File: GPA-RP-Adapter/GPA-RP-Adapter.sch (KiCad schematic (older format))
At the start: 8 parts

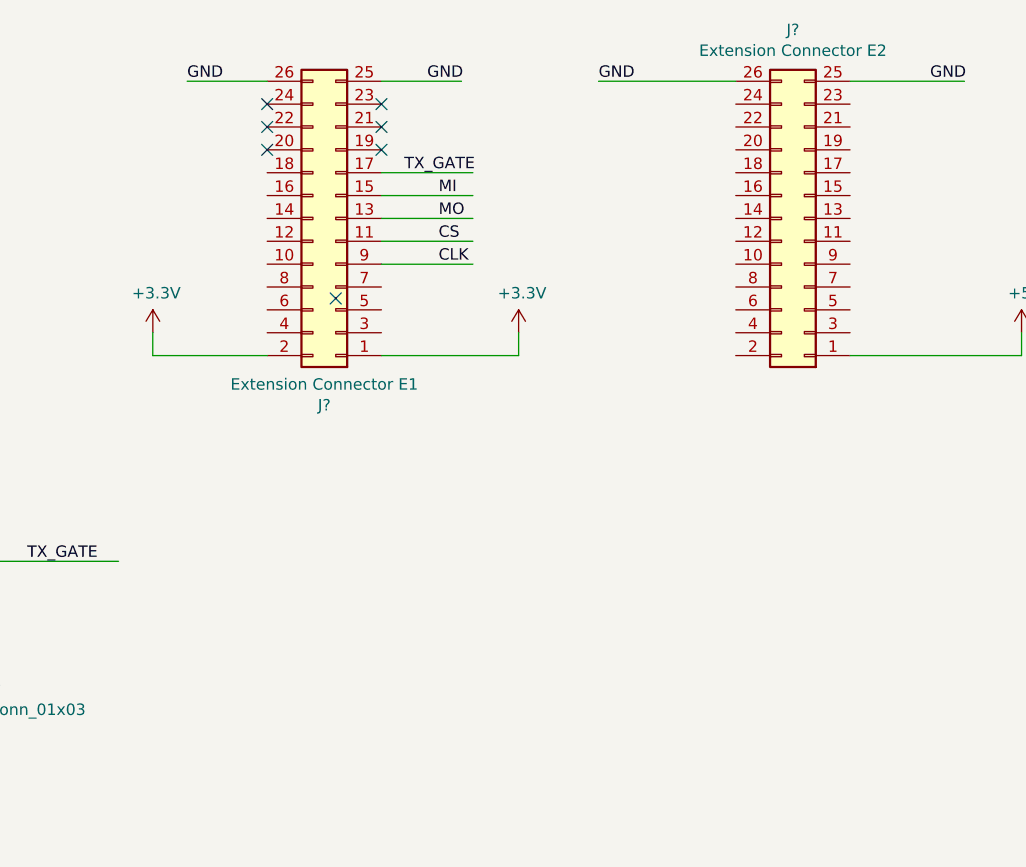
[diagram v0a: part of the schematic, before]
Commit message: added 2nd tx_gate
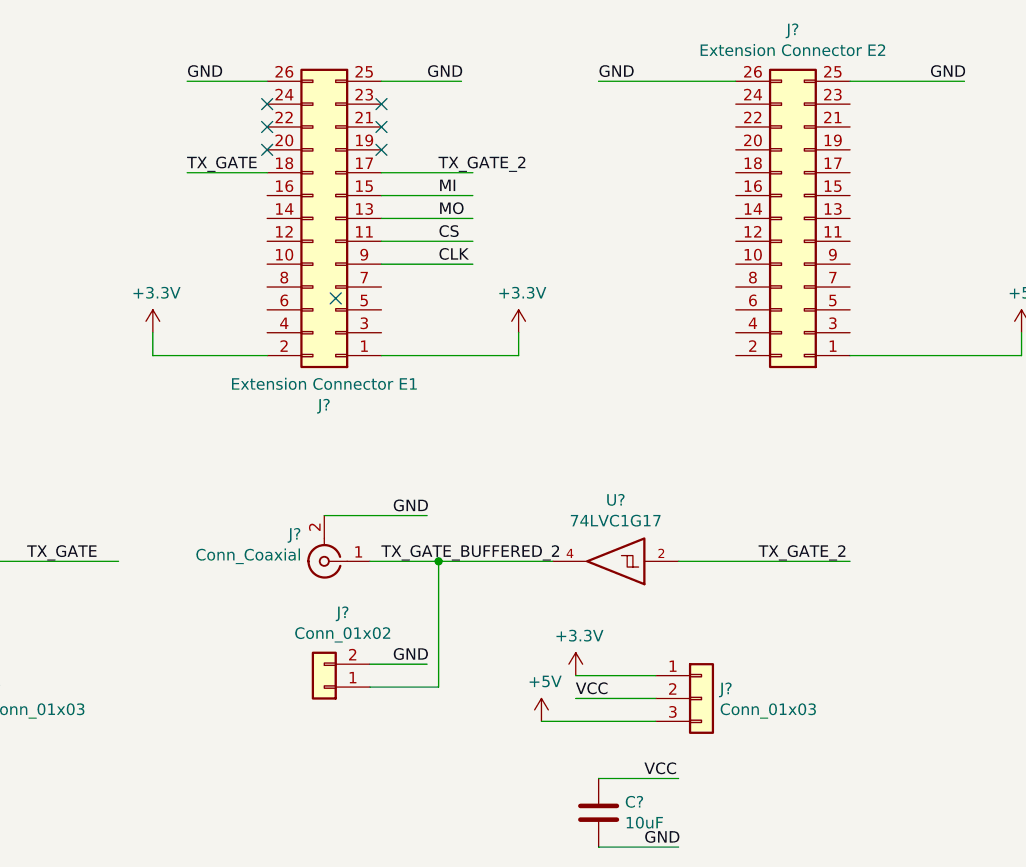
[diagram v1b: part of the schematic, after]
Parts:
- added C?: 10uF, symbol Device:C
- added J?: Conn_Coaxial, symbol Connector:Conn_Coaxial
- added J?: Conn_01x03, symbol Connector_Generic:Conn_01x03
- added J?: Conn_01x02, symbol Connector_Generic:Conn_01x02
- added U?: 74LVC1G17, symbol 74xGxx:74LVC1G17
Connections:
- net labels added: TX_GATE_2, TX_GATE_BUFFERED_2
- wire segments 38 -> 51
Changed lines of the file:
@@
 Text Label 1550 3200 0    50   ~ 0
 TX_GATE_BUFFERED
-Wire Wire Line
-	4750 1500 5150 1500
-Text Label 4850 1500 0    50   ~ 0
-TX_GATE
 $Comp
 L 74xGxx:74LVC1G17 U?
@@
 Wire Wire Line
 	1800 3200 2300 3200
+Wire Wire Line
+	4250 1500 3900 1500
+Text Label 3900 1500 0    50   ~ 0
+TX_GATE
+Wire Wire Line
+	4750 1500 5150 1500
+Text Label 5000 1500 0    50   ~ 0
+TX_GATE_2
+$Comp
+L Connector:Conn_Coaxial J?
+U 1 1 5F8539A5
+P 4500 3200
+F 0 "J?" H 4600 3082 50  0000 L CNN
+F 1 "Conn_Coaxial" H 4600 3173 50  0000 L CNN
+F 2 "" H 4500 3200 50  0001 C CNN
+F 3 " ~" H 4500 3200 50  0001 C CNN
+	1    4500 3200
+	-1   0    0    1
+$EndComp
+Wire Wire Line
+	4500 3000 4950 3000
+Text Label 4800 3000 0    50   ~ 0
+GND
+Text Label 4750 3200 0    50   ~ 0
+TX_GATE_BUFFERED_2
+$Comp
+L 74xGxx:74LVC1G17 U?
+U 1 1 5F8539AE
+P 5750 3200
+F 0 "U?" H 5725 2933 50  0000 C CNN
+F 1 "74LVC1G17" H 5725 3024 50  0000 C CNN
+F 2 "" H 5750 3200 50  0001 C CNN
+F 3 "http://www.ti.com/lit/sg/scyt129e/scyt129e.pdf" H 5750 3200 50  0001 C CNN
+	1    5750 3200
+	-1   0    0    1
+$EndComp
+Wire Wire Line
+	6050 3200 6800 3200
+Text Label 6400 3200 0    50   ~ 0
+TX_GATE_2
+$Comp
+L Connector_Generic:Conn_01x03 J?
+U 1 1 5F8539B6
+P 6150 3800
+F 0 "J?" H 6230 3842 50  0000 L CNN
+F 1 "Conn_01x03" H 6230 3751 50  0000 L CNN
+F 2 "" H 6150 3800 50  0001 C CNN
+F 3 "~" H 6150 3800 50  0001 C CNN
+	1    6150 3800
+	1    0    0    -1
+$EndComp
+Wire Wire Line
+	5950 3800 5600 3800
+Text Label 5600 3800 0    50   ~ 0
+VCC
+Wire Wire Line
+	5950 3700 5600 3700
+$Comp
+L power:+3.3V #PWR?
+U 1 1 5F8539BF
+P 5600 3700
+F 0 "#PWR?" H 5600 3550 50  0001 C CNN
+F 1 "+3.3V" H 5615 3873 50  0000 C CNN
+F 2 "" H 5600 3700 50  0001 C CNN
+F 3 "" H 5600 3700 50  0001 C CNN
+	1    5600 3700
+	1    0    0    -1
+$EndComp
+$Comp
+L power:+5V #PWR?
+U 1 1 5F8539C5
+P 5450 3900
+F 0 "#PWR?" H 5450 3750 50  0001 C CNN
+F 1 "+5V" H 5465 4073 50  0000 C CNN
+F 2 "" H 5450 3900 50  0001 C CNN
+F 3 "" H 5450 3900 50  0001 C CNN
+	1    5450 3900
+	1    0    0    -1
+$EndComp
+Wire Wire Line
+	5450 3900 5950 3900
+$Comp
+L Device:C C?
+U 1 1 5F8539CC
+P 5700 4300
+F 0 "C?" H 5815 4346 50  0000 L CNN
+F 1 "10uF" H 5815 4255 50  0000 L CNN
+F 2 "" H 5738 4150 50  0001 C CNN
+F 3 "~" H 5700 4300 50  0001 C CNN
+	1    5700 4300
+	1    0    0    -1
+$EndComp
+Wire Wire Line
+	5700 4150 6050 4150
+Wire Wire Line
+	5700 4450 6050 4450
+Text Label 5900 4150 0    50   ~ 0
+VCC
+Text Label 5900 4450 0    50   ~ 0
+GND
+$Comp
+L Connector_Generic:Conn_01x02 J?
+U 1 1 5F8539D6
+P 4500 3750
+F 0 "J?" H 4418 3425 50  0000 C CNN
+F 1 "Conn_01x02" H 4418 3516 50  0000 C CNN
+F 2 "" H 4500 3750 50  0001 C CNN
+F 3 "~" H 4500 3750 50  0001 C CNN
+	1    4500 3750
+	-1   0    0    1
+$EndComp
+Wire Wire Line
+	4700 3750 5000 3750
+Wire Wire Line
+	4700 3650 4950 3650
+Text Label 4800 3650 0    50   ~ 0
+GND
+Wire Wire Line
+	5000 3750 5000 3200
+Wire Wire Line
+	4700 3200 5000 3200
+Connection ~ 5000 3200
+Wire Wire Line
+	5000 3200 5500 3200
 $EndSCHEMATC

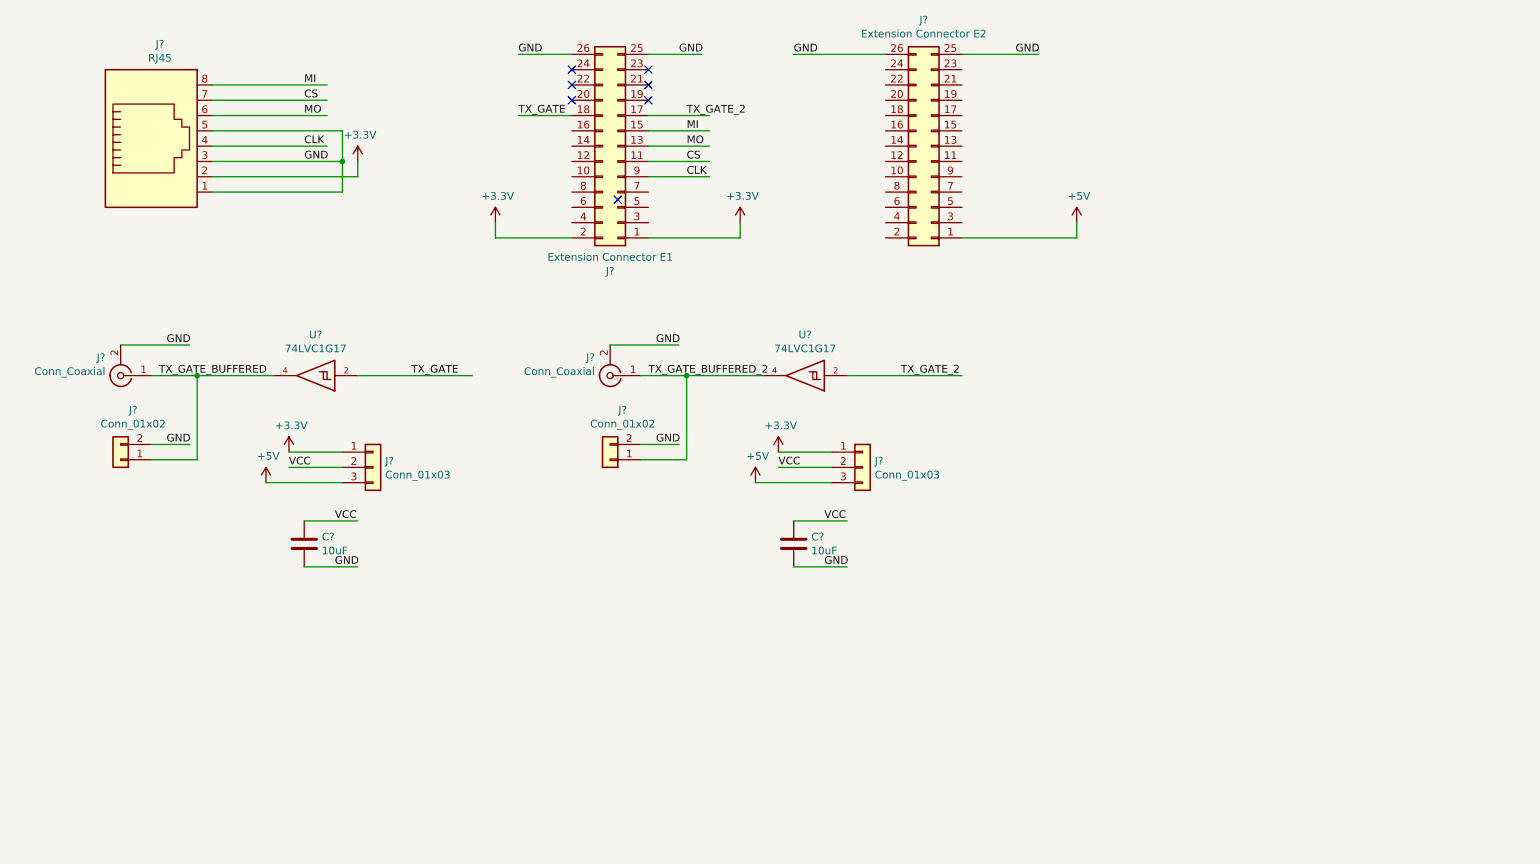
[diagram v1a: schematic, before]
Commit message: added analog IOs, SPI and fan
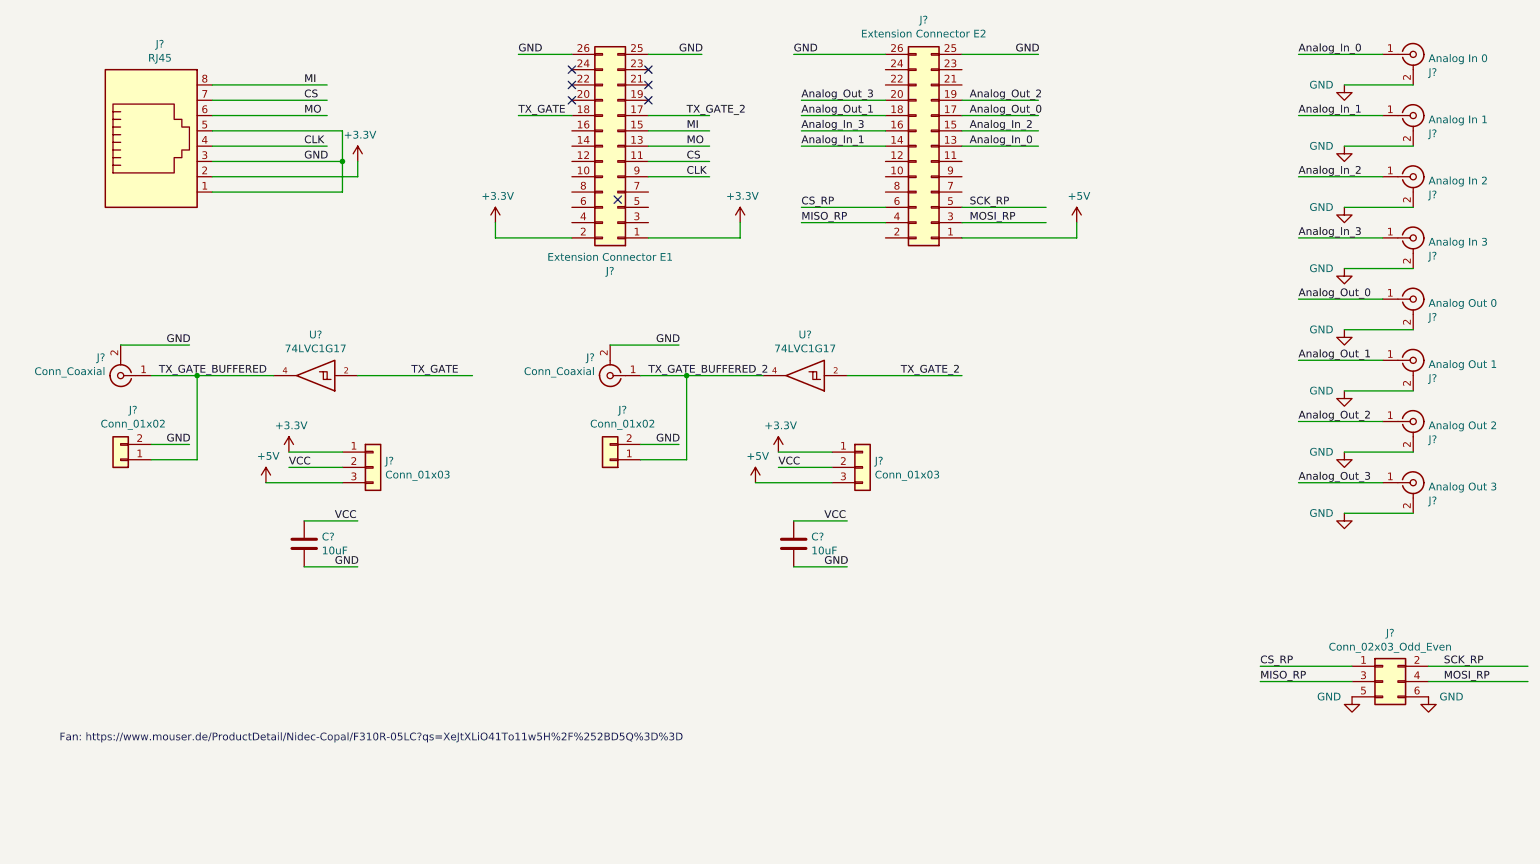
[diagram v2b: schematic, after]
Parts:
- added J?: Analog In 0, symbol Connector:Conn_Coaxial
- added J?: Analog In 1, symbol Connector:Conn_Coaxial
- added J?: Analog In 2, symbol Connector:Conn_Coaxial
- added J?: Analog In 3, symbol Connector:Conn_Coaxial
- added J?: Analog Out 0, symbol Connector:Conn_Coaxial
- added J?: Analog Out 1, symbol Connector:Conn_Coaxial
- added J?: Analog Out 2, symbol Connector:Conn_Coaxial
- added J?: Analog Out 3, symbol Connector:Conn_Coaxial
- added J?: Conn_02x03_Odd_Even, symbol Connector_Generic:Conn_02x03_Odd_Even
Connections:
- net labels added: Analog_In_0, Analog_In_1, Analog_In_2, Analog_In_3, Analog_Out_0, Analog_Out_1, Analog_Out_2, Analog_Out_3, CS_RP, MISO_RP, MOSI_RP, SCK_RP
- wire segments 51 -> 83
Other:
- note added: "Fan: https://www.mouser.de/ProductDetail/Nidec-Copal/F310R-05LC?qs=XeJtXLiO41To11w5H%2F%252BD5Q%3D%3D"

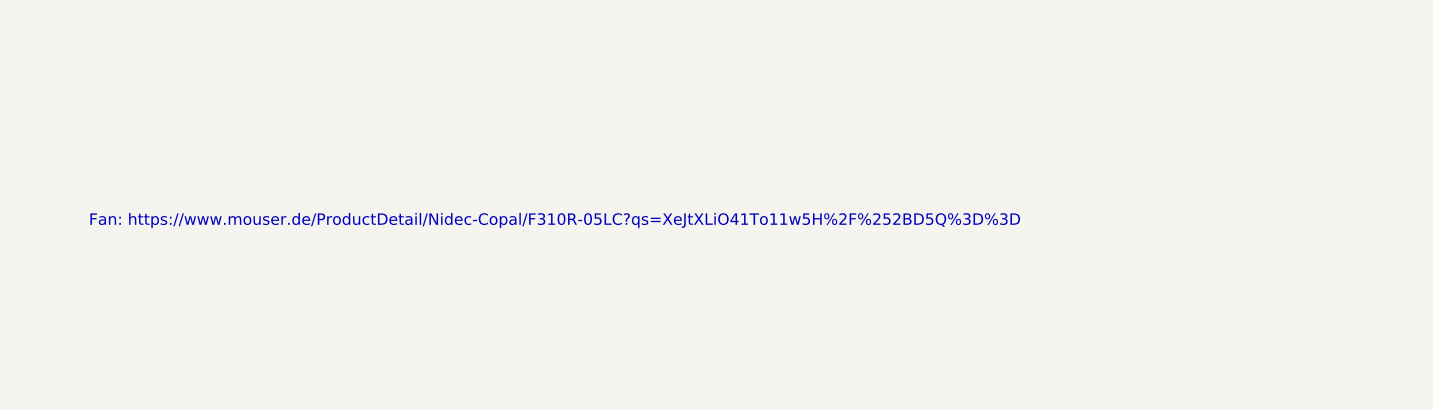
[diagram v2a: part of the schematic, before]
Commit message: added PWR connector for fan
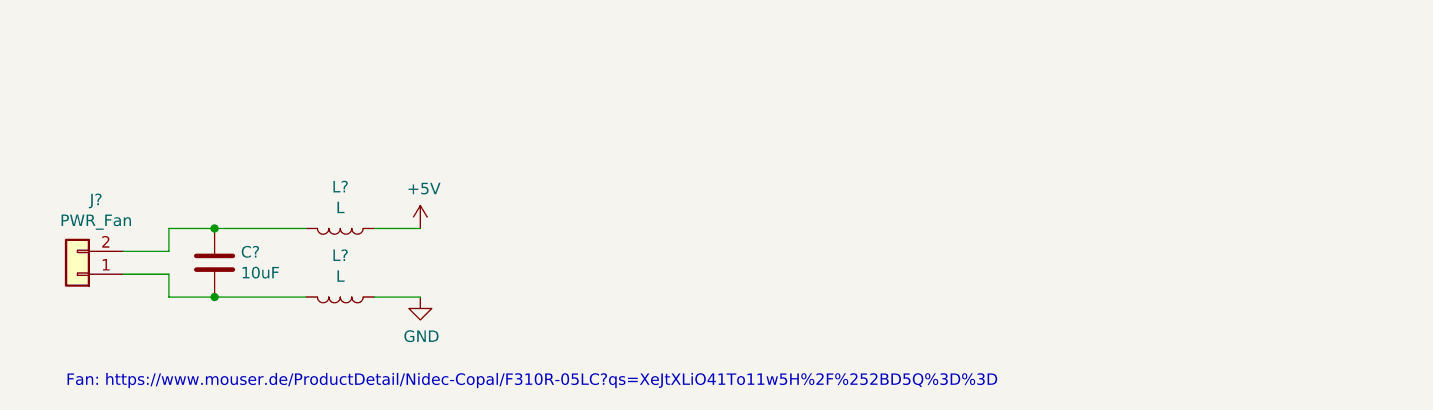
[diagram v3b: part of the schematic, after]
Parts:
- added C?: 10uF, symbol Device:C
- added J?: PWR_Fan, symbol Connector_Generic:Conn_01x02
- added L? (x2): L, symbol Device:L
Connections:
- wire segments 83 -> 93
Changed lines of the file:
@@
 	1    0    0    -1
 $EndComp
-Text Notes 900  5600 0    50   ~ 0
+Text Notes 800  6300 0    50   ~ 0
 Fan: https://www.mouser.de/ProductDetail/Nidec-Copal/F310R-05LC?qs=XeJtXLiO41To11w5H%2F%252BD5Q%3D%3D
+$Comp
+L Connector_Generic:Conn_01x02 J?
+U 1 1 5F8527DE
+P 850 5800
+F 0 "J?" H 768 5475 50  0000 C CNN
+F 1 "PWR_Fan" H 768 5566 50  0000 C CNN
+F 2 "" H 850 5800 50  0001 C CNN
+F 3 "~" H 850 5800 50  0001 C CNN
+	1    850  5800
+	-1   0    0    1
+$EndComp
+$Comp
+L Device:C C?
+U 1 1 5F859B5B
+P 1450 5750
+F 0 "C?" H 1565 5796 50  0000 L CNN
+F 1 "10uF" H 1565 5705 50  0000 L CNN
+F 2 "" H 1488 5600 50  0001 C CNN
+F 3 "~" H 1450 5750 50  0001 C CNN
+	1    1450 5750
+	1    0    0    -1
+$EndComp
+Wire Wire Line
+	1450 5900 1250 5900
+Wire Wire Line
+	1250 5900 1250 5800
+Wire Wire Line
+	1250 5800 1050 5800
+Wire Wire Line
+	1050 5700 1250 5700
+Wire Wire Line
+	1250 5700 1250 5600
+Wire Wire Line
+	1250 5600 1450 5600
+$Comp
+L Device:L L?
+U 1 1 5F868675
+P 2000 5600
+F 0 "L?" V 1819 5600 50  0000 C CNN
+F 1 "L" V 1910 5600 50  0000 C CNN
+F 2 "" H 2000 5600 50  0001 C CNN
+F 3 "~" H 2000 5600 50  0001 C CNN
+	1    2000 5600
+	0    1    1    0
+$EndComp
+$Comp
+L Device:L L?
+U 1 1 5F869FCB
+P 2000 5900
+F 0 "L?" V 1819 5900 50  0000 C CNN
+F 1 "L" V 1910 5900 50  0000 C CNN
+F 2 "" H 2000 5900 50  0001 C CNN
+F 3 "~" H 2000 5900 50  0001 C CNN
+	1    2000 5900
+	0    1    1    0
+$EndComp
+Wire Wire Line
+	1850 5600 1450 5600
+Connection ~ 1450 5600
+Wire Wire Line
+	1450 5900 1850 5900
+Connection ~ 1450 5900
+$Comp
+L power:GND #PWR?
+U 1 1 5F8773B6
+P 2350 5900
+F 0 "#PWR?" H 2350 5650 50  0001 C CNN
+F 1 "GND" H 2355 5727 50  0000 C CNN
+F 2 "" H 2350 5900 50  0001 C CNN
+F 3 "" H 2350 5900 50  0001 C CNN
+	1    2350 5900
+	1    0    0    -1
+$EndComp
+Wire Wire Line
+	2150 5900 2350 5900
+Wire Wire Line
+	2150 5600 2350 5600
+$Comp
+L power:+5V #PWR?
+U 1 1 5F8825B5
+P 2350 5600
+F 0 "#PWR?" H 2350 5450 50  0001 C CNN
+F 1 "+5V" H 2365 5773 50  0000 C CNN
+F 2 "" H 2350 5600 50  0001 C CNN
+F 3 "" H 2350 5600 50  0001 C CNN
+	1    2350 5600
+	1    0    0    -1
+$EndComp
 $EndSCHEMATC

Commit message: finished layout
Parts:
- removed J?: Analog In 2, symbol Connector:Conn_Coaxial
- removed J?: Analog In 3, symbol Connector:Conn_Coaxial
- removed J?: Analog Out 2, symbol Connector:Conn_Coaxial
- removed J?: Analog Out 3, symbol Connector:Conn_Coaxial
- C1, C2, C3: renamed from C?; footprint (none) -> Capacitor_SMD:C_0805_2012Metric_Pad1.15x1.40mm_HandSolder
- J1, J3, J7: renamed from J?; footprint (none) -> Connector_PinHeader_2.54mm:PinHeader_1x02_P2.54mm_Vertical
- J10, J8: renamed from J?; footprint (none) -> Connector_PinHeader_2.54mm:PinHeader_2x13_P2.54mm_Vertical
- J11: renamed from J?; footprint (none) -> Connector_PinHeader_2.54mm:PinHeader_2x03_P2.54mm_Vertical
- J12, J13, J16, J17, J2, J6: renamed from J?; footprint (none) -> Connector_Coaxial:SMA_Amphenol_132134_Vertical
- J4: renamed from J?; footprint (none) -> Connector_RJ:RJ45_Amphenol_54602-x08_Horizontal
- J5, J9: renamed from J?; footprint (none) -> Connector_PinHeader_2.54mm:PinHeader_1x03_P2.54mm_Vertical
- L1, L2: renamed from L?; footprint (none) -> Inductor_SMD:L_0805_2012Metric_Pad1.15x1.40mm_HandSolder
- U1, U2: renamed from U?; footprint (none) -> Package_TO_SOT_SMD:SOT-23-5_HandSoldering; symbol 74xGxx:74LVC1G17 -> user_Logic:74LVC1G17
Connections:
- net labels added: VCC1, VCC2
- net labels removed: VCC
- wire segments 93 -> 89
